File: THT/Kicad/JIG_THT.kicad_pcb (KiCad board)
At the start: 2 copper layers, 54.6 x 66 mm, 12 parts

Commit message: On of the silkscreen text was off centered
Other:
- board text added: "5V ONLY (OPT.)"
- board text removed: "5V ONLY (OPT)"
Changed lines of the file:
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@@
     (effects (font (size 1 1) (thickness 0.2) bold) (justify left bottom mirror))
   )
-  (gr_text "5V ONLY (OPT)" (at 76.2 88.9 90) (layer "F.SilkS")
+  (gr_text "5V ONLY (OPT.)" (at 76.2 92.5 90) (layer "F.SilkS")
     (effects (font (size 1 1) (thickness 0.2)) (justify left bottom))
   )

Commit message: Removed D-/D+ labels
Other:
- board text added: "RX"
- board text added: "TX"
- board text removed: "RX/D+"
- board text removed: "TX/D-"
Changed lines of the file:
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@@
     (effects (font (size 1 1) (thickness 0.2)) (justify left bottom))
   )
-  (gr_text "TX/D-" (at 81.28 63.5) (layer "F.SilkS")
+  (gr_text "TX" (at 81.28 63.5) (layer "F.SilkS")
     (effects (font (size 1 1) (thickness 0.15)))
   )
@@
     (effects (font (size 2 2) (thickness 0.4) bold) (justify left bottom))
   )
-  (gr_text "RX/D+" (at 81.28 71.12) (layer "F.SilkS")
+  (gr_text "RX" (at 81.28 71.12) (layer "F.SilkS")
     (effects (font (size 1 1) (thickness 0.15)))
   )

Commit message: fixed issues pertaining to k-line schematics
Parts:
- moved 1n4148 12.7 mm to (61.0, 62.0), turned to 0 degrees
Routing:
- net (no net): track 319.4 -> 299.5 mm, vias 6 -> 5
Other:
- board text added: "PSP GO THT JIG BOARD 1.1 By Mathieulh"
- board text removed: "PSP GO THT JIG BOARD 1.0 By Mathieulh"
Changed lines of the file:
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@@
   )
   (footprint "Diode_THT:D_5W_P12.70mm_Horizontal" (layer "F.Cu")
-    (at 73.66 62 180)
+    (at 60.96 62)
     (descr "Diode, 5W series, Axial, Horizontal, pin pitch=12.7mm, , length*diameter=8.9*3.7mm^2, , http://www.diodes.com/_files/packages/8686949.gif")
     (tags "Diode 5W series Axial Horizontal pin pitch 12.7mm  length 8.9mm diameter 3.7mm")
@@
     (fp_line (start 12.7 0) (end 10.8 0)
       (stroke (width 0.1) (type solid)) (layer "F.Fab"))
-    (pad "1" thru_hole rect (at 0 0 180) (size 2.8 2.8) (drill 1.4) (layers "*.Cu" "*.Mask"))
-    (pad "2" thru_hole oval (at 12.7 0 180) (size 2.8 2.8) (drill 1.4) (layers "*.Cu" "*.Mask"))
+    (pad "1" thru_hole rect (at 0 0) (size 2.8 2.8) (drill 1.4) (layers "*.Cu" "*.Mask"))
+    (pad "2" thru_hole oval (at 12.7 0) (size 2.8 2.8) (drill 1.4) (layers "*.Cu" "*.Mask"))
     (model "${KICAD6_3DMODEL_DIR}/Diode_THT.3dshapes/D_5W_P12.70mm_Horizontal.wrl"
       (offset (xyz 0 0 0))
@@
     (effects (font (size 2 2) (thickness 0.4) bold) (justify left bottom))
   )
-  (gr_text "PSP GO THT JIG BOARD 1.0\nBy Mathieulh" (at 43.18 55.88) (layer "F.SilkS")
+  (gr_text "PSP GO THT JIG BOARD 1.1\nBy Mathieulh" (at 43.18 55.88) (layer "F.SilkS")
     (effects (font (size 1.5 1.5) (thickness 0.3) bold) (justify left bottom))
   )
@@
   (segment (start 81.28 76.2) (end 50.8 76.2) (width 0.25) (layer "F.Cu") (net 0))
   (segment (start 43.18 53.34) (end 43.18 45.72) (width 0.25) (layer "F.Cu") (net 0))
-  (segment (start 73.66 66.04) (end 76.2 63.5) (width 0.25) (layer "F.Cu") (net 0))
-  (segment (start 76.2 63.5) (end 78.74 60.96) (width 0.25) (layer "F.Cu") (net 0))
   (segment (start 58.42 68.58) (end 50.8 76.2) (width 0.25) (layer "F.Cu") (net 0))
+  (segment (start 73.66 62) (end 74.7 62) (width 0) (layer "F.Cu") (net 0))
   (segment (start 48.26 58.42) (end 48.26 63.5) (width 0.25) (layer "F.Cu") (net 0))
   (segment (start 38.1 78.74) (end 38.1 83.82) (width 0.25) (layer "F.Cu") (net 0))
-  (segment (start 75.16 63.5) (end 73.66 62) (width 0.25) (layer "F.Cu") (net 0))
   (segment (start 48.26 60.96) (end 48.26 58.42) (width 0.25) (layer "F.Cu") (net 0))
   (segment (start 55.88 45.72) (end 58.42 45.72) (width 0.25) (layer "F.Cu") (net 0))
   (segment (start 50.8 93.98) (end 38.1 93.98) (width 0.25) (layer "F.Cu") (net 0))
   (segment (start 48.26 58.42) (end 43.18 53.34) (width 0.25) (layer "F.Cu") (net 0))
+  (segment (start 74.7 62) (end 81.28 68.58) (width 0.25) (layer "F.Cu") (net 0))
   (segment (start 48.26 68.58) (end 38.1 78.74) (width 0.25) (layer "F.Cu") (net 0))
   (segment (start 50.8 76.2) (end 50.8 93.98) (width 0.25) (layer "F.Cu") (net 0))
@@
   (segment (start 81.28 91.44) (end 81.28 83.82) (width 0.25) (layer "F.Cu") (net 0))
   (segment (start 76.2 91.44) (end 81.28 91.44) (width 0.25) (layer "F.Cu") (net 0))
-  (segment (start 76.2 63.5) (end 75.16 63.5) (width 0.25) (layer "F.Cu") (net 0))
-  (segment (start 78.74 68.58) (end 81.28 68.58) (width 0.25) (layer "F.Cu") (net 0))
+  (segment (start 81.28 60.96) (end 81.28 68.58) (width 0.25) (layer "F.Cu") (net 0))
   (segment (start 64.002056 103.637944) (end 76.2 91.44) (width 0.25) (layer "F.Cu") (net 0))
+  (segment (start 73.66 66.04) (end 78.74 66.04) (width 0.25) (layer "F.Cu") (net 0))
   (segment (start 38.1 103.637944) (end 64.002056 103.637944) (width 0.25) (layer "F.Cu") (net 0))
   (segment (start 58.42 58.42) (end 71.12 45.72) (width 0.25) (layer "F.Cu") (net 0))
-  (segment (start 78.74 60.96) (end 81.28 60.96) (width 0.25) (layer "F.Cu") (net 0))
-  (segment (start 63.5 45.72) (end 58.42 45.72) (width 0) (layer "F.Cu") (net 0))
+  (segment (start 63.5 45.72) (end 58.42 45.72) (width 0.25) (layer "F.Cu") (net 0))
   (segment (start 38.1 71.12) (end 38.1 73.66) (width 0.25) (layer "F.Cu") (net 0))
   (segment (start 71.12 45.72) (end 76.2 45.72) (width 0.25) (layer "F.Cu") (net 0))
@@
   (segment (start 43.18 66.04) (end 66.04 66.04) (width 0.25) (layer "F.Cu") (net 0))
   (segment (start 58.42 45.72) (end 58.42 50.8) (width 0.25) (layer "F.Cu") (net 0))
+  (segment (start 78.74 66.04) (end 81.28 68.58) (width 0.25) (layer "F.Cu") (net 0))
   (segment (start 43.18 66.04) (end 38.1 71.12) (width 0.25) (layer "F.Cu") (net 0))
   (via (at 58.42 68.58) (size 0.6) (drill 0.3) (layers "F.Cu" "B.Cu") (net 0))
@@
   (via (at 48.26 63.5) (size 0.6) (drill 0.3) (layers "F.Cu" "B.Cu") (net 0))
   (via (at 58.42 63.5) (size 0.6) (drill 0.3) (layers "F.Cu" "B.Cu") (net 0))
-  (via (at 78.74 68.58) (size 0.6) (drill 0.3) (layers "F.Cu" "B.Cu") (net 0))
-  (segment (start 71.12 55.88) (end 78.74 63.5) (width 0.25) (layer "B.Cu") (net 0))
-  (segment (start 78.74 63.5) (end 78.74 68.58) (width 0.25) (layer "B.Cu") (net 0))
-  (segment (start 71.12 55.88) (end 65 62) (width 0.25) (layer "B.Cu") (net 0))
-  (segment (start 58.42 50.8) (end 66.04 50.8) (width 0.25) (layer "B.Cu") (net 0))
-  (segment (start 65 62) (end 60.96 62) (width 0.25) (layer "B.Cu") (net 0))
+  (segment (start 58.42 50.8) (end 60.96 53.34) (width 0.25) (layer "B.Cu") (net 0))
   (segment (start 48.26 63.5) (end 48.26 68.58) (width 0.25) (layer "B.Cu") (net 0))
   (segment (start 58.42 63.5) (end 58.42 68.58) (width 0.25) (layer "B.Cu") (net 0))
-  (segment (start 66.04 50.8) (end 71.12 55.88) (width 0.25) (layer "B.Cu") (net 0))
+  (segment (start 60.96 53.34) (end 60.96 62) (width 0.25) (layer "B.Cu") (net 0))
 )

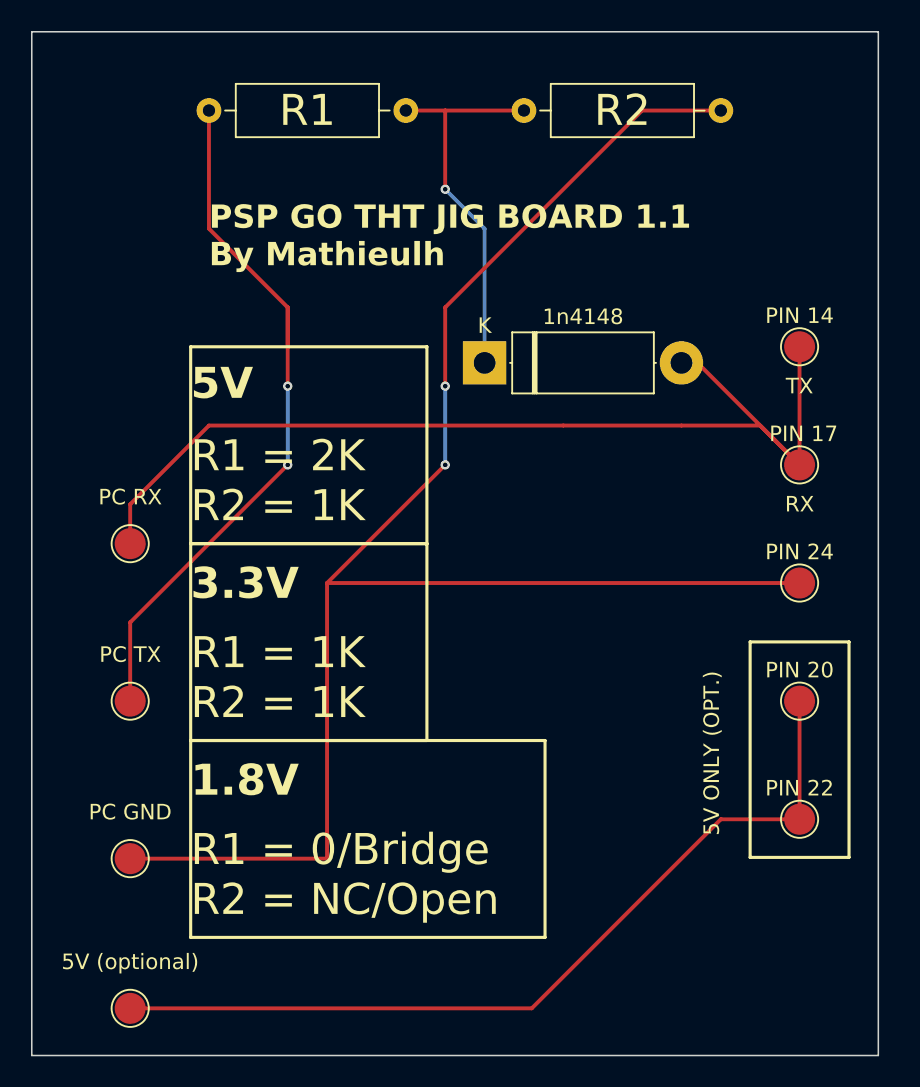
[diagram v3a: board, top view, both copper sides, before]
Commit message: Fixed PIN24
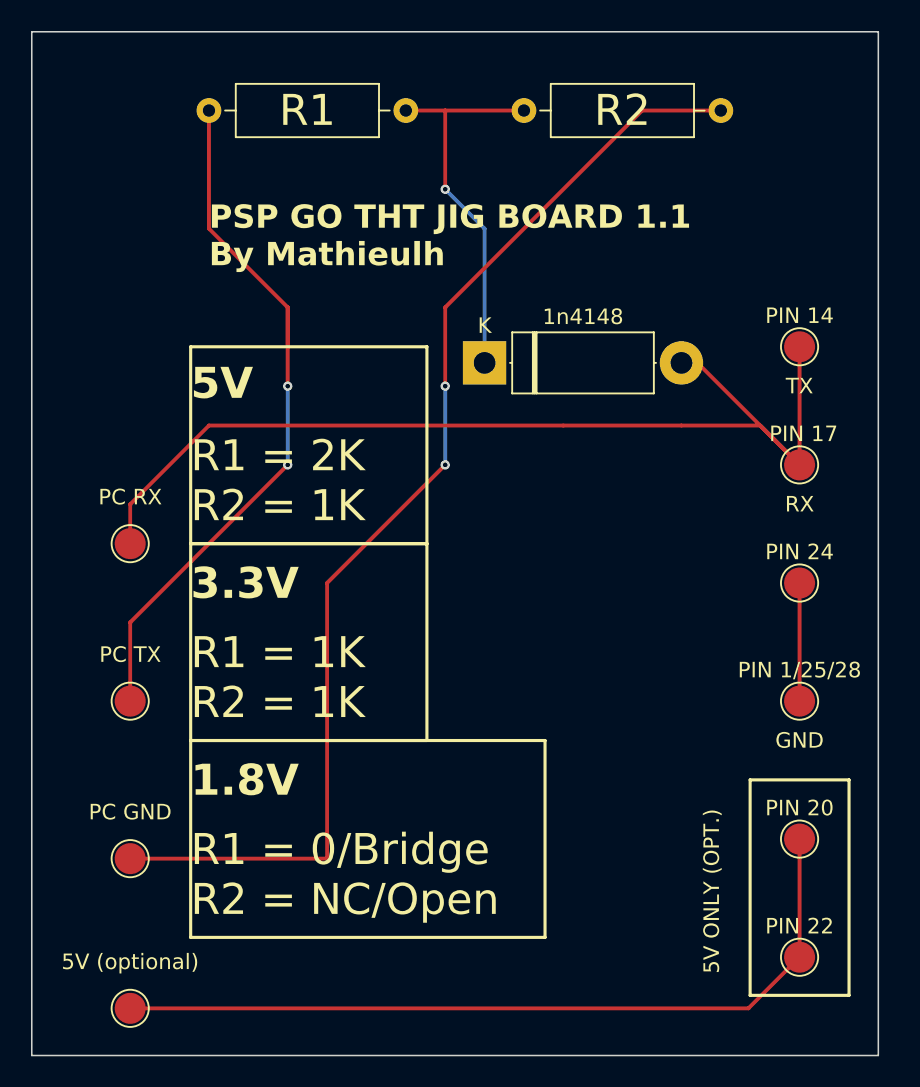
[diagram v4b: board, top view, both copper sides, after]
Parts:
- added PIN 1/25/28: TestPoint_Pad_D2.0mm, TestPoint:TestPoint_Pad_D2.0mm, F.Cu at (81.3, 83.8)
- moved PIN 20 8.90 mm to (81.3, 92.7)
- moved PIN 22 8.90 mm to (81.3, 100.3)
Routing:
- net (no net): track 299.5 -> 273.0 mm
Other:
- board text added: "GND"
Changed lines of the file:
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@@
   (net 0 "")
+  (footprint "TestPoint:TestPoint_Pad_D2.0mm" (layer "F.Cu")
+    (at 81.28 83.82)
+    (descr "SMD pad as test Point, diameter 2.0mm")
+    (tags "test point SMD pad")
+    (attr exclude_from_pos_files exclude_from_bom)
+    (fp_text reference "PIN 1/25/28" (at 0 -1.998) (layer "F.SilkS")
+        (effects (font (size 1 1) (thickness 0.15)))
+    )
+    (fp_text value "TestPoint_Pad_D2.0mm" (at 0 2.05) (layer "F.Fab")
+        (effects (font (size 1 1) (thickness 0.15)))
+    )
+    (fp_text user "${REFERENCE}" (at 0 -2) (layer "F.Fab")
+        (effects (font (size 1 1) (thickness 0.15)))
+    )
+    (fp_circle (center 0 0) (end 0 1.2)
+      (stroke (width 0.12) (type solid)) (fill none) (layer "F.SilkS"))
+    (fp_circle (center 0 0) (end 1.5 0)
+      (stroke (width 0.05) (type solid)) (fill none) (layer "F.CrtYd"))
+    (pad "8" smd circle (at 0 0) (size 2 2) (layers "F.Cu" "F.Mask"))
+  )
   (footprint "TestPoint:TestPoint_Pad_D2.0mm" (layer "F.Cu")
     (at 81.28 76.2)
@@
   )
   (footprint "TestPoint:TestPoint_Pad_D2.0mm" (layer "F.Cu")
-    (at 81.28 83.82)
+    (at 81.28 92.72)
     (descr "SMD pad as test Point, diameter 2.0mm")
     (tags "test point SMD pad")
@@
     (fp_circle (center 0 0) (end 1.5 0)
       (stroke (width 0.05) (type solid)) (fill none) (layer "F.CrtYd"))
-    (pad "8" smd circle (at 0 0) (size 2 2) (layers "F.Cu" "F.Mask"))
+    (pad "9" smd circle (at 0 0) (size 2 2) (layers "F.Cu" "F.Mask"))
   )
   (footprint "TestPoint:TestPoint_Pad_D2.0mm" (layer "F.Cu")
@@
   )
   (footprint "TestPoint:TestPoint_Pad_D2.0mm" (layer "F.Cu")
-    (at 81.28 91.44)
+    (at 81.28 100.34)
     (descr "SMD pad as test Point, diameter 2.0mm")
     (tags "test point SMD pad")
@@
     (fp_circle (center 0 0) (end 1.5 0)
       (stroke (width 0.05) (type solid)) (fill none) (layer "F.CrtYd"))
-    (pad "9" smd circle (at 0 0) (size 2 2) (layers "F.Cu" "F.Mask"))
+    (pad "10" smd circle (at 0 0) (size 2 2) (layers "F.Cu" "F.Mask"))
   )
   (footprint "TestPoint:TestPoint_Pad_D2.0mm" (layer "F.Cu")
@@
   (gr_rect (start 42 73.66) (end 57.24 86.36)
     (stroke (width 0.2) (type default)) (fill none) (layer "F.SilkS"))
-  (gr_rect (start 78.09 80) (end 84.47 93.9)
+  (gr_rect (start 78.09 88.9) (end 84.47 102.8)
     (stroke (width 0.2) (type default)) (fill none) (layer "F.SilkS"))
   (gr_rect (start 31.75 40.64) (end 86.36 106.68)
@@
     (effects (font (size 1 1) (thickness 0.2) bold) (justify left bottom mirror))
   )
-  (gr_text "5V ONLY (OPT.)" (at 76.2 92.5 90) (layer "F.SilkS")
+  (gr_text "5V ONLY (OPT.)" (at 76.2 101.4 90) (layer "F.SilkS")
     (effects (font (size 1 1) (thickness 0.2)) (justify left bottom))
+  )
+  (gr_text "GND" (at 81.28 86.36) (layer "F.SilkS")
+    (effects (font (size 1 1) (thickness 0.15)))
   )
   (gr_text "TX" (at 81.28 63.5) (layer "F.SilkS")
@@
     (effects (font (size 2 2) (thickness 0.4) bold) (justify left bottom))
   )
-  (segment (start 81.28 76.2) (end 50.8 76.2) (width 0.25) (layer "F.Cu") (net 0))
   (segment (start 43.18 53.34) (end 43.18 45.72) (width 0.25) (layer "F.Cu") (net 0))
   (segment (start 58.42 68.58) (end 50.8 76.2) (width 0.25) (layer "F.Cu") (net 0))
@@
   (segment (start 48.26 58.42) (end 43.18 53.34) (width 0.25) (layer "F.Cu") (net 0))
   (segment (start 74.7 62) (end 81.28 68.58) (width 0.25) (layer "F.Cu") (net 0))
+  (segment (start 77.982056 103.637944) (end 38.1 103.637944) (width 0.25) (layer "F.Cu") (net 0))
   (segment (start 48.26 68.58) (end 38.1 78.74) (width 0.25) (layer "F.Cu") (net 0))
   (segment (start 50.8 76.2) (end 50.8 93.98) (width 0.25) (layer "F.Cu") (net 0))
   (segment (start 58.42 63.5) (end 58.42 58.42) (width 0.25) (layer "F.Cu") (net 0))
-  (segment (start 81.28 91.44) (end 81.28 83.82) (width 0.25) (layer "F.Cu") (net 0))
-  (segment (start 76.2 91.44) (end 81.28 91.44) (width 0.25) (layer "F.Cu") (net 0))
+  (segment (start 81.28 76.2) (end 81.28 83.82) (width 0.25) (layer "F.Cu") (net 0))
+  (segment (start 81.28 100.34) (end 81.28 92.72) (width 0.25) (layer "F.Cu") (net 0))
   (segment (start 81.28 60.96) (end 81.28 68.58) (width 0.25) (layer "F.Cu") (net 0))
-  (segment (start 64.002056 103.637944) (end 76.2 91.44) (width 0.25) (layer "F.Cu") (net 0))
   (segment (start 73.66 66.04) (end 78.74 66.04) (width 0.25) (layer "F.Cu") (net 0))
-  (segment (start 38.1 103.637944) (end 64.002056 103.637944) (width 0.25) (layer "F.Cu") (net 0))
+  (segment (start 81.28 100.34) (end 77.982056 103.637944) (width 0.25) (layer "F.Cu") (net 0))
   (segment (start 58.42 58.42) (end 71.12 45.72) (width 0.25) (layer "F.Cu") (net 0))
   (segment (start 63.5 45.72) (end 58.42 45.72) (width 0.25) (layer "F.Cu") (net 0))

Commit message: Cleanup + fix GND
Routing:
- net (no net): track 273.0 -> 303.5 mm
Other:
- board text added: "PSP GO THT JIG BOARD 1.2 By Mathieulh"
- board text removed: "PSP GO THT JIG BOARD 1.1 By Mathieulh"
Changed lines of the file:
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@@
     (effects (font (size 2 2) (thickness 0.4) bold) (justify left bottom))
   )
-  (gr_text "PSP GO THT JIG BOARD 1.1\nBy Mathieulh" (at 43.18 55.88) (layer "F.SilkS")
+  (gr_text "PSP GO THT JIG BOARD 1.2\nBy Mathieulh" (at 43.18 55.88) (layer "F.SilkS")
     (effects (font (size 1.5 1.5) (thickness 0.3) bold) (justify left bottom))
   )
@@
   (segment (start 63.5 45.72) (end 58.42 45.72) (width 0.25) (layer "F.Cu") (net 0))
   (segment (start 38.1 71.12) (end 38.1 73.66) (width 0.25) (layer "F.Cu") (net 0))
+  (segment (start 81.28 83.82) (end 50.8 83.82) (width 0.25) (layer "F.Cu") (net 0))
   (segment (start 71.12 45.72) (end 76.2 45.72) (width 0.25) (layer "F.Cu") (net 0))
   (segment (start 66.04 66.04) (end 73.66 66.04) (width 0.25) (layer "F.Cu") (net 0))

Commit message: Fix PIN 20
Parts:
- added 10KR: R_Axial_DIN0309_L9.0mm_D3.2mm_P12.70mm_Horizontal, Resistor_THT:R_Axial_DIN0309_L9.0mm_D3.2mm_P12.70mm_Horizontal, F.Cu at (57.1, 101.6)
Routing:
- net (no net): track 303.5 -> 330.9 mm
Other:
- board text added: "PSP GO THT JIG BOARD 1.3 By Mathieulh"
- board text removed: "PSP GO THT JIG BOARD 1.2 By Mathieulh"
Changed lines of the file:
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@@
+  )
+  (footprint "Resistor_THT:R_Axial_DIN0309_L9.0mm_D3.2mm_P12.70mm_Horizontal" (layer "F.Cu")
+    (at 57.15 101.6)
+    (descr "Resistor, Axial_DIN0309 series, Axial, Horizontal, pin pitch=12.7mm, 0.5W = 1/2W, length*diameter=9*3.2mm^2, http://cdn-reichelt.de/documents/datenblatt/B400/1_4W%23YAG.pdf")
+    (tags "Resistor Axial_DIN0309 series Axial Horizontal pin pitch 12.7mm 0.5W = 1/2W length 9mm diameter 3.2mm")
+    (attr through_hole)
+    (fp_text reference "10KR" (at 6.35 0) (layer "F.SilkS")
+        (effects (font (size 2 2) (thickness 0.3)))
+    )
+    (fp_text value "R_Axial_DIN0309_L9.0mm_D3.2mm_P12.70mm_Horizontal" (at 6.35 2.72) (layer "F.Fab")
+        (effects (font (size 1 1) (thickness 0.15)))
+    )
+    (fp_text user "${REFERENCE}" (at 6.35 0) (layer "F.Fab")
+        (effects (font (size 1 1) (thickness 0.15)))
+    )
+    (fp_line (start 1.04 0) (end 1.73 0)
+      (stroke (width 0.12) (type solid)) (layer "F.SilkS"))
+    (fp_line (start 1.73 -1.72) (end 1.73 1.72)
+      (stroke (width 0.12) (type solid)) (layer "F.SilkS"))
+    (fp_line (start 1.73 1.72) (end 10.97 1.72)
+      (stroke (width 0.12) (type solid)) (layer "F.SilkS"))
+    (fp_line (start 10.97 -1.72) (end 1.73 -1.72)
+      (stroke (width 0.12) (type solid)) (layer "F.SilkS"))
+    (fp_line (start 10.97 1.72) (end 10.97 -1.72)
+      (stroke (width 0.12) (type solid)) (layer "F.SilkS"))
+    (fp_line (start 11.66 0) (end 10.97 0)
+      (stroke (width 0.12) (type solid)) (layer "F.SilkS"))
+    (fp_line (start -1.05 -1.85) (end -1.05 1.85)
+      (stroke (width 0.05) (type solid)) (layer "F.CrtYd"))
+    (fp_line (start -1.05 1.85) (end 13.75 1.85)
+      (stroke (width 0.05) (type solid)) (layer "F.CrtYd"))
+    (fp_line (start 13.75 -1.85) (end -1.05 -1.85)
+      (stroke (width 0.05) (type solid)) (layer "F.CrtYd"))
+    (fp_line (start 13.75 1.85) (end 13.75 -1.85)
+      (stroke (width 0.05) (type solid)) (layer "F.CrtYd"))
+    (fp_line (start 0 0) (end 1.85 0)
+      (stroke (width 0.1) (type solid)) (layer "F.Fab"))
+    (fp_line (start 1.85 -1.6) (end 1.85 1.6)
+      (stroke (width 0.1) (type solid)) (layer "F.Fab"))
+    (fp_line (start 1.85 1.6) (end 10.85 1.6)
+      (stroke (width 0.1) (type solid)) (layer "F.Fab"))
+    (fp_line (start 10.85 -1.6) (end 1.85 -1.6)
+      (stroke (width 0.1) (type solid)) (layer "F.Fab"))
+    (fp_line (start 10.85 1.6) (end 10.85 -1.6)
+      (stroke (width 0.1) (type solid)) (layer "F.Fab"))
+    (fp_line (start 12.7 0) (end 10.85 0)
+      (stroke (width 0.1) (type solid)) (layer "F.Fab"))
+    (pad "1" thru_hole circle (at 0 0) (size 1.6 1.6) (drill 0.8) (layers "*.Cu" "*.Mask"))
+    (pad "2" thru_hole oval (at 12.7 0) (size 1.6 1.6) (drill 0.8) (layers "*.Cu" "*.Mask"))
+    (model "${KICAD6_3DMODEL_DIR}/Resistor_THT.3dshapes/R_Axial_DIN0309_L9.0mm_D3.2mm_P12.70mm_Horizontal.wrl"
+      (offset (xyz 0 0 0))
+      (scale (xyz 1 1 1))
+      (rotate (xyz 0 0 0))
+    )
   )
   (footprint "Resistor_THT:R_Axial_DIN0309_L9.0mm_D3.2mm_P12.70mm_Horizontal" (layer "F.Cu")
@@
     (effects (font (size 2 2) (thickness 0.4) bold) (justify left bottom))
   )
-  (gr_text "PSP GO THT JIG BOARD 1.2\nBy Mathieulh" (at 43.18 55.88) (layer "F.SilkS")
+  (gr_text "PSP GO THT JIG BOARD 1.3\nBy Mathieulh" (at 43.18 55.88) (layer "F.SilkS")
     (effects (font (size 1.5 1.5) (thickness 0.3) bold) (justify left bottom))
   )
@@
     (effects (font (size 2 2) (thickness 0.4) bold) (justify left bottom))
   )
+  (segment (start 40.137944 101.6) (end 57.15 101.6) (width 0.25) (layer "F.Cu") (net 0))
   (segment (start 43.18 53.34) (end 43.18 45.72) (width 0.25) (layer "F.Cu") (net 0))
   (segment (start 58.42 68.58) (end 50.8 76.2) (width 0.25) (layer "F.Cu") (net 0))
   (segment (start 73.66 62) (end 74.7 62) (width 0) (layer "F.Cu") (net 0))
   (segment (start 48.26 58.42) (end 48.26 63.5) (width 0.25) (layer "F.Cu") (net 0))
+  (segment (start 38.1 103.637944) (end 40.137944 101.6) (width 0.25) (layer "F.Cu") (net 0))
   (segment (start 38.1 78.74) (end 38.1 83.82) (width 0.25) (layer "F.Cu") (net 0))
   (segment (start 48.26 60.96) (end 48.26 58.42) (width 0.25) (layer "F.Cu") (net 0))
+  (segment (start 81.28 92.72) (end 78.73 92.72) (width 0.25) (layer "F.Cu") (net 0))
   (segment (start 55.88 45.72) (end 58.42 45.72) (width 0.25) (layer "F.Cu") (net 0))
   (segment (start 50.8 93.98) (end 38.1 93.98) (width 0.25) (layer "F.Cu") (net 0))
@@
   (segment (start 58.42 63.5) (end 58.42 58.42) (width 0.25) (layer "F.Cu") (net 0))
   (segment (start 81.28 76.2) (end 81.28 83.82) (width 0.25) (layer "F.Cu") (net 0))
-  (segment (start 81.28 100.34) (end 81.28 92.72) (width 0.25) (layer "F.Cu") (net 0))
   (segment (start 81.28 60.96) (end 81.28 68.58) (width 0.25) (layer "F.Cu") (net 0))
   (segment (start 73.66 66.04) (end 78.74 66.04) (width 0.25) (layer "F.Cu") (net 0))
@@
   (segment (start 81.28 83.82) (end 50.8 83.82) (width 0.25) (layer "F.Cu") (net 0))
   (segment (start 71.12 45.72) (end 76.2 45.72) (width 0.25) (layer "F.Cu") (net 0))
+  (segment (start 78.73 92.72) (end 69.85 101.6) (width 0.25) (layer "F.Cu") (net 0))
   (segment (start 66.04 66.04) (end 73.66 66.04) (width 0.25) (layer "F.Cu") (net 0))
   (segment (start 43.18 66.04) (end 66.04 66.04) (width 0.25) (layer "F.Cu") (net 0))
